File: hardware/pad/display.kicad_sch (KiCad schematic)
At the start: 6 parts, among them J6 OLED 1.3in SPI, U8 TPS22919DCK

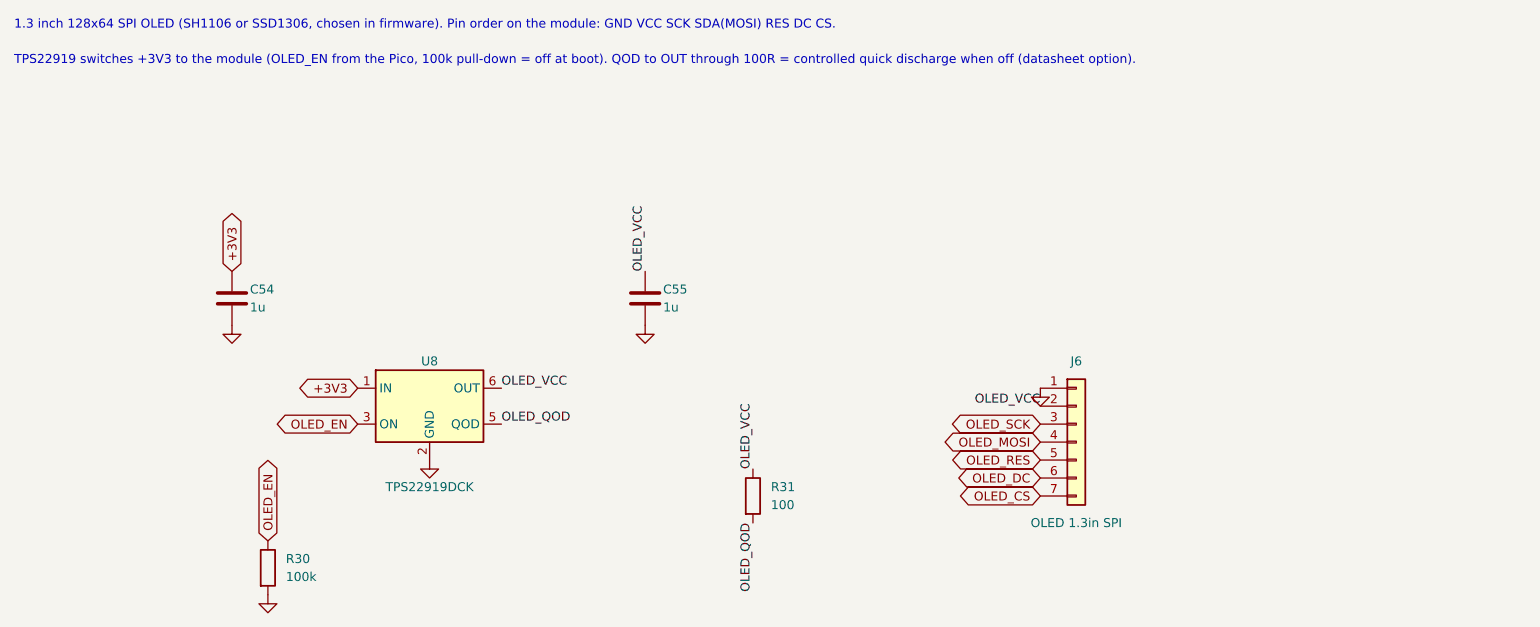
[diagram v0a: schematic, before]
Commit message: Pad schematic: hand-redrawn from the connection guide; netlist verified against the reference
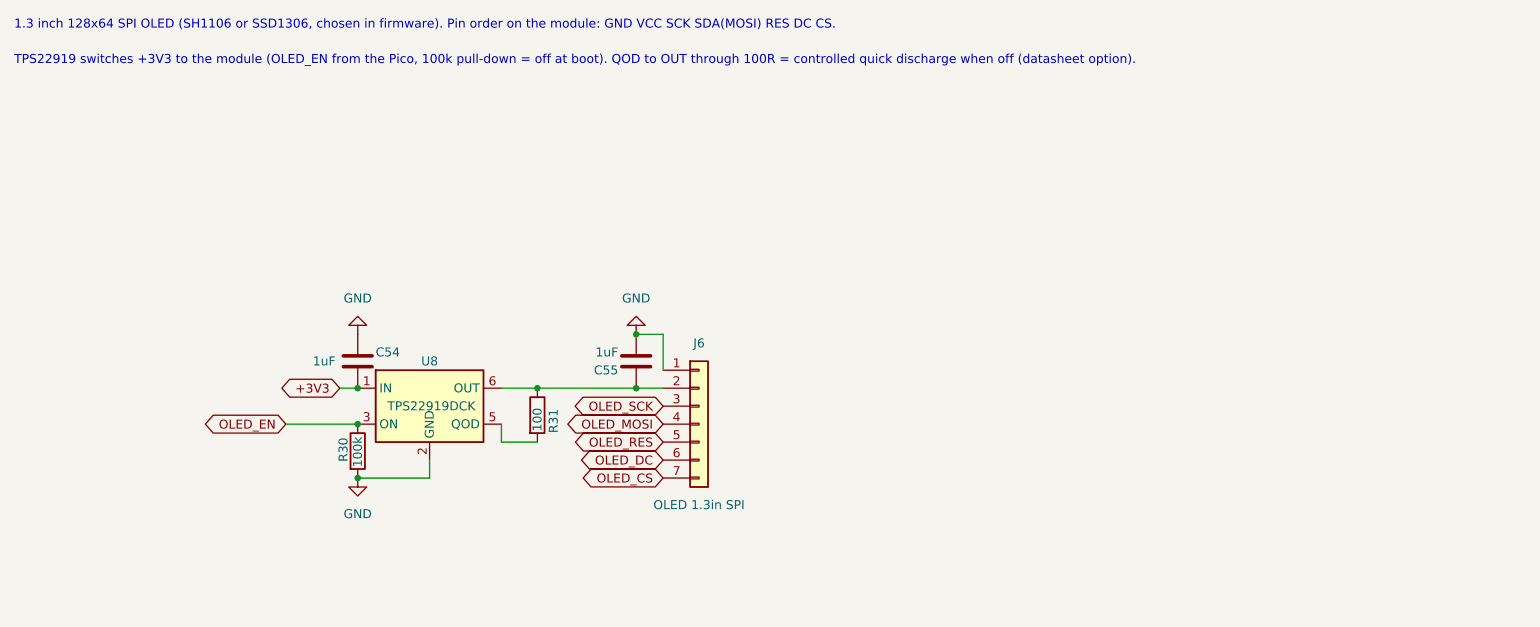
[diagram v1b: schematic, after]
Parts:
- C54, C55: value 1u -> 1uF
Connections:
- net +3V3: now also C54.2; no longer C54.1
- net GND: now also C54.1; no longer C54.2
- net OLED_QOD: no longer names the net of R31.2, U8.5 (QOD)
- net OLED_VCC: no longer names the net of C55.1, J6.2 (Pin_2), R31.1, U8.6 (OUT)
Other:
- moved on the sheet: C55, J6
